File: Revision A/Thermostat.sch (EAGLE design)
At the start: 22 parts

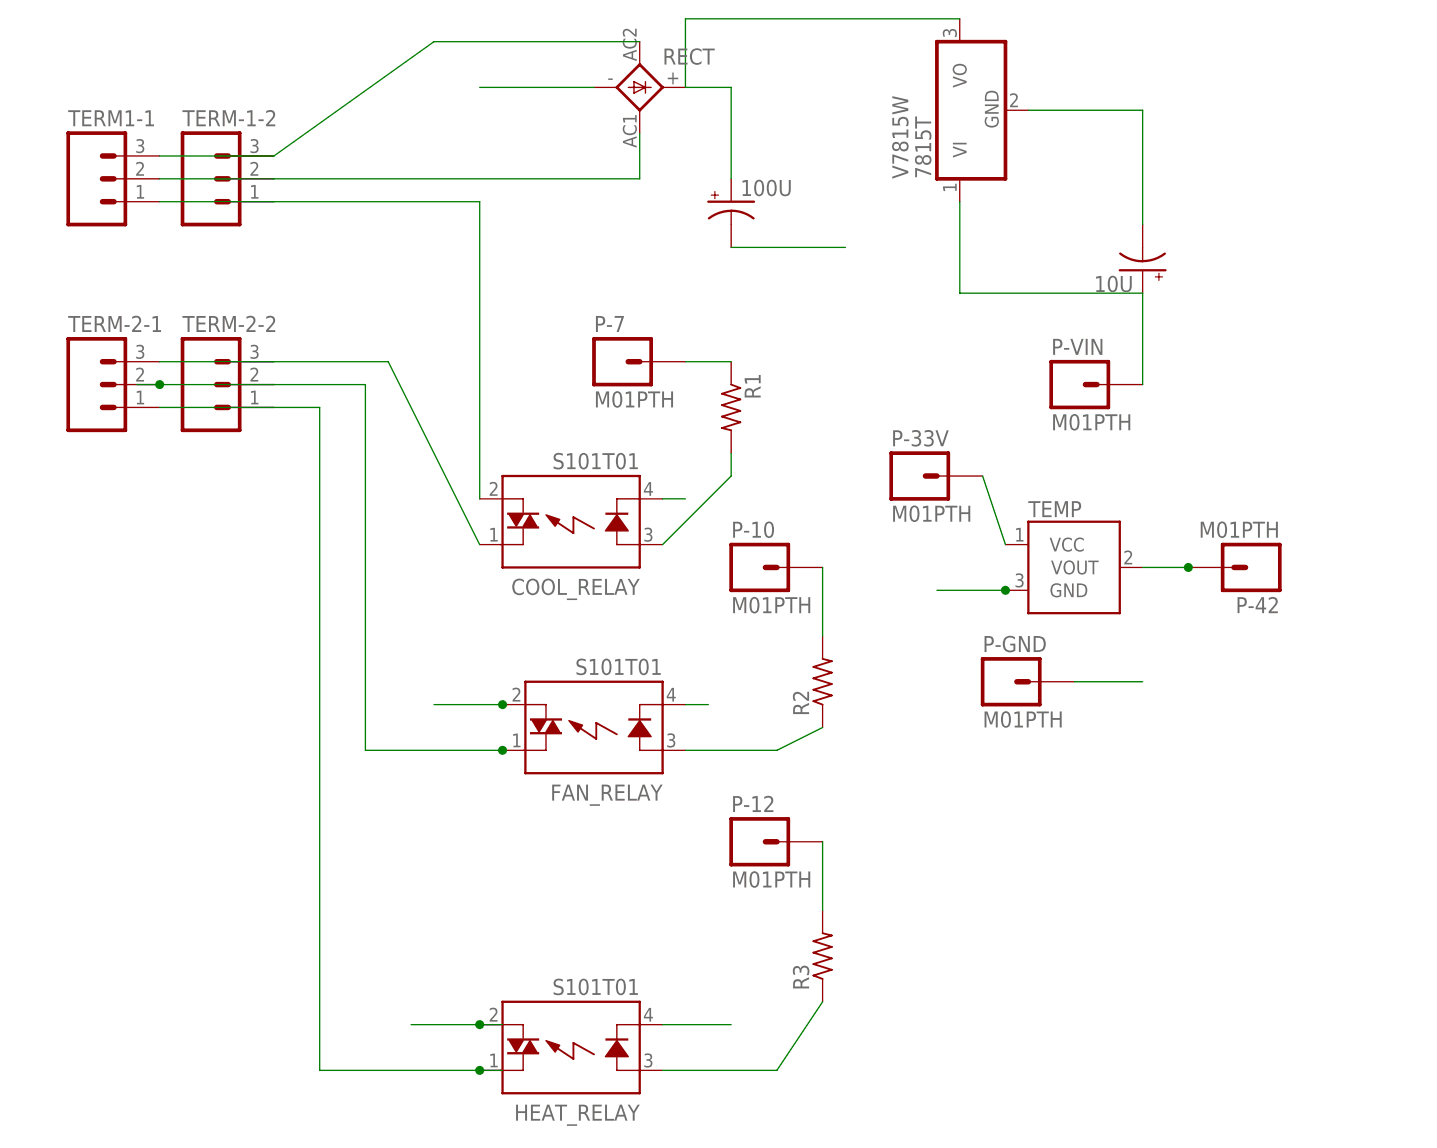
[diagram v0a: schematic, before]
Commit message: Custom Components
Designed custom components for the temperature sensor and switching
regulator.  Corrected pin 42 to 46.  Corrected some mistakes in the
schematic and re-arranged it.  Rewired the board paths to match the
original published directions.  Have not tested printing or alignment
yet.
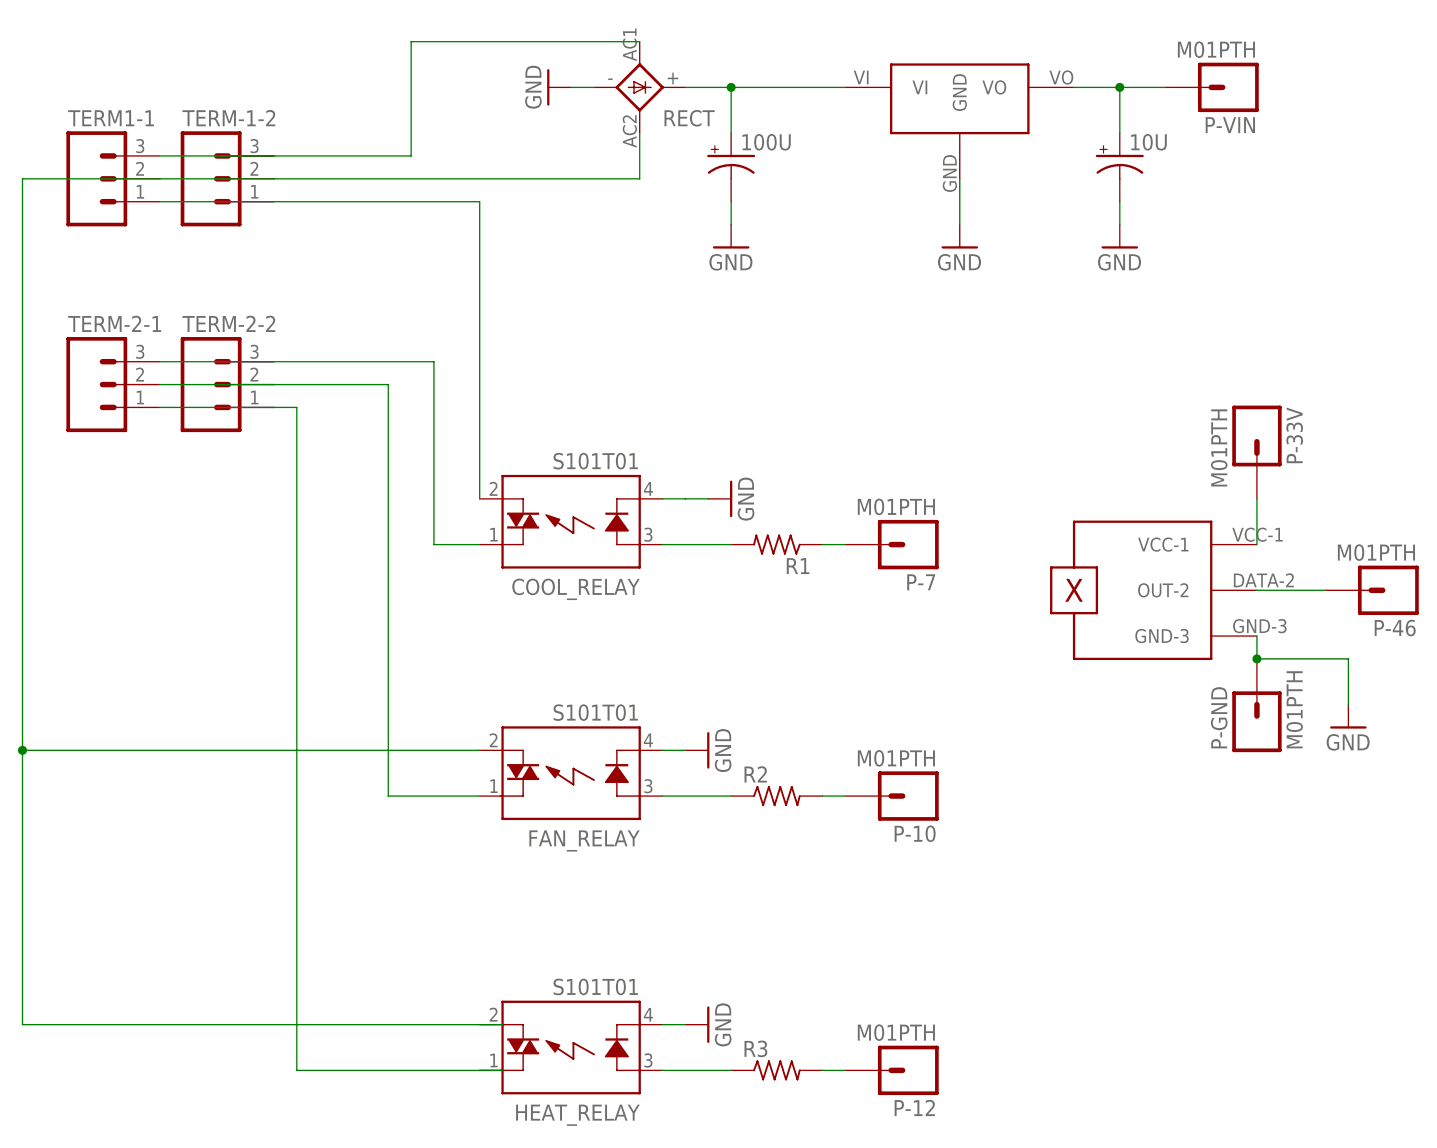
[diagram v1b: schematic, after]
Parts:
- removed P-42: M01PTH, SparkFun-Connectors:M01PTH
- removed TEMP: (no value), SparkFun-Sensors:TMP36GT9
- removed V7815W: 7815T, linear:7815T
- added P-46: M01PTH, SparkFun-Connectors:M01PTH
- added U$1: TMP36, android-thermostat:TMP36
- added U$2: V715W-500R, android-thermostat:V715W-500R
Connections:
- removed net N$13 (its old number): 100U.+, RECT.+, V7815W.VO
- new net N$5: P-46.1, U$1.OUT-2
- net GND: now also U$1.GND-3, U$2.GND; no longer TEMP.GND, V7815W.GND
- net N$10: now also 10U.+, P-VIN.1, U$2.VO; no longer P-42.1, TEMP.VOUT
- net N$11: now also U$1.VCC-1; no longer TEMP.VCC
- net N$12: now also 100U.+, RECT.+, U$2.VI; no longer 10U.+, P-VIN.1, V7815W.VI
- net N$3: now also RECT.AC2; no longer RECT.AC1
- net P2: now also RECT.AC1; no longer RECT.AC2
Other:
- moved on the sheet: 100U, 10U, FAN_RELAY, P-10, P-12, P-33V, P-7, P-GND, P-VIN, R1, R2, R3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
